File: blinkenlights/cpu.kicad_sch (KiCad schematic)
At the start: 13 parts, among them J501 Conn_ARM_SWD, J502 USB4085-GF-A_REVA4, U501 ATSAM4S8CB-AN, U502 PCA9306DP

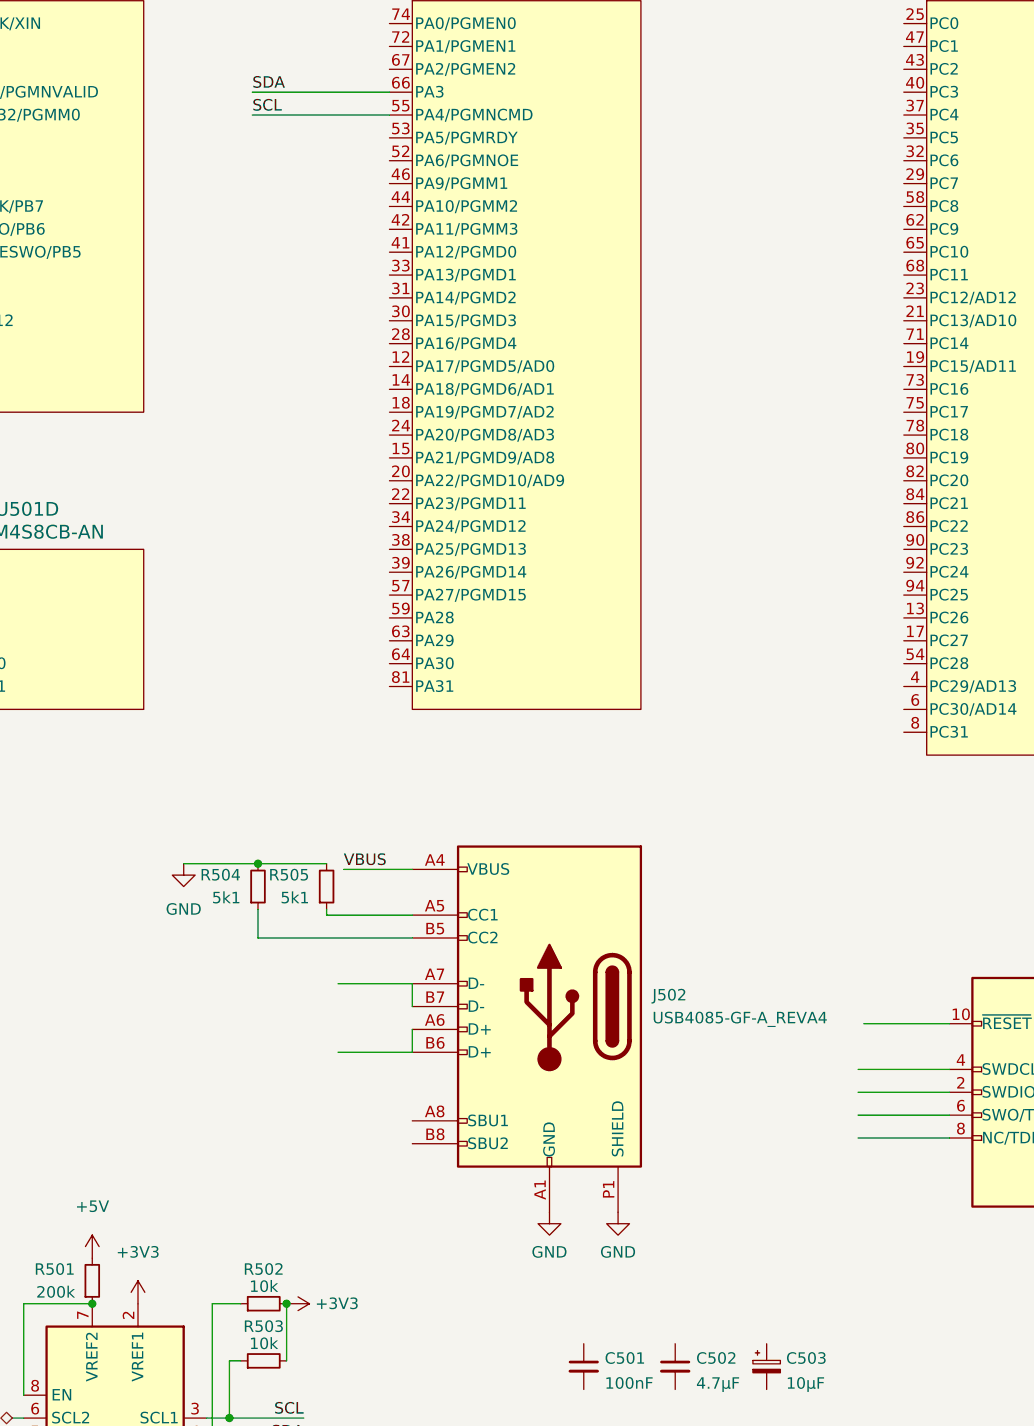
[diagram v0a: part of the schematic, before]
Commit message: removed usb that shit's whack yo
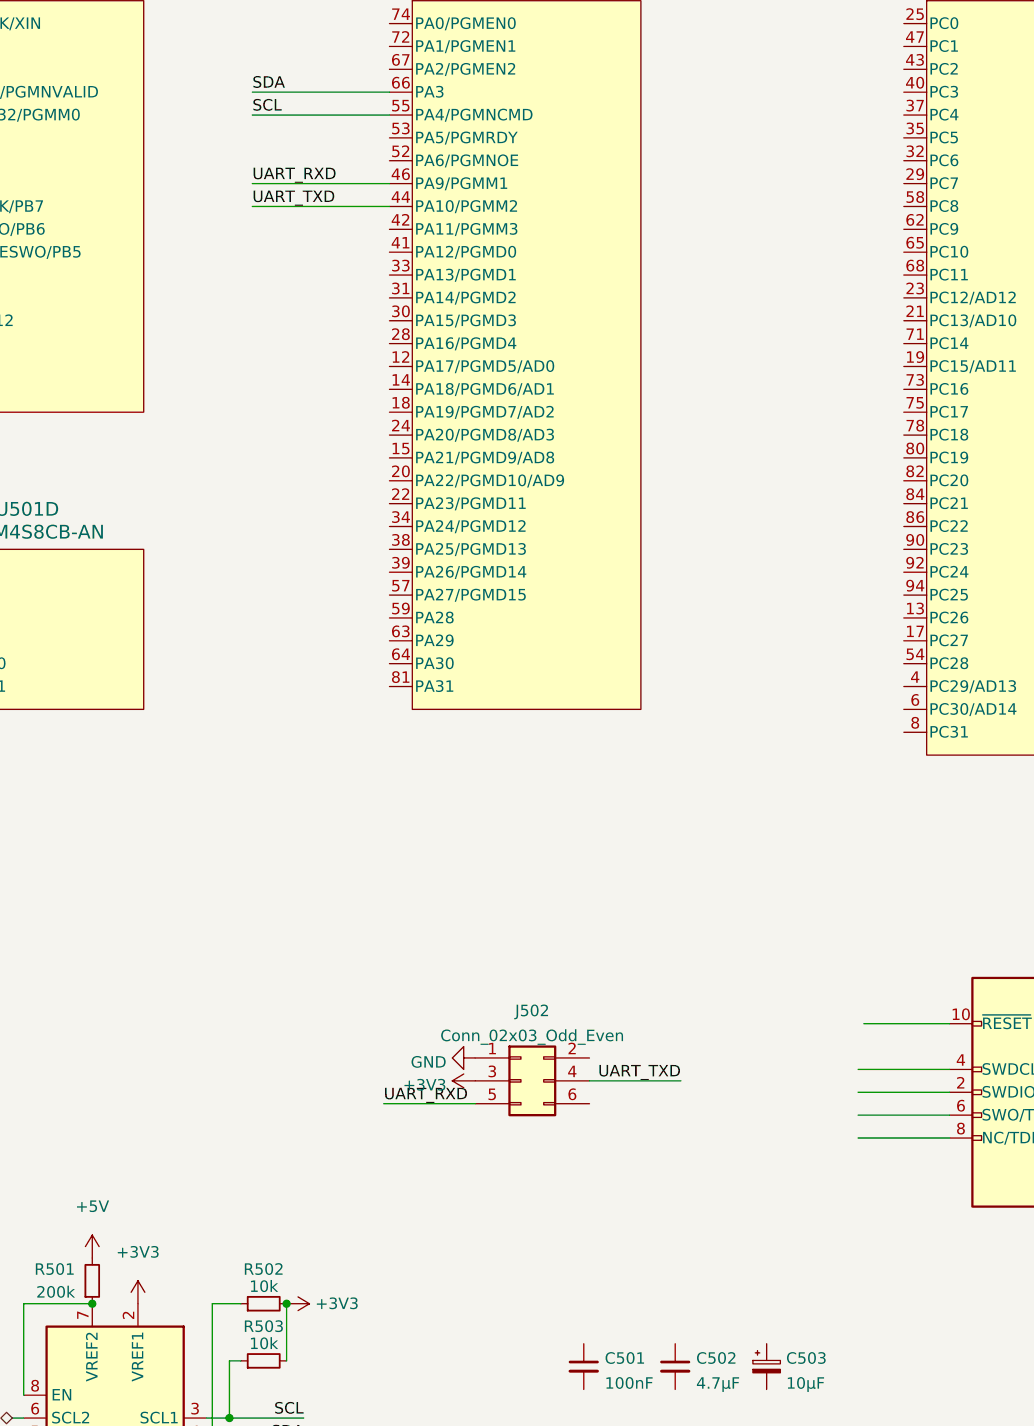
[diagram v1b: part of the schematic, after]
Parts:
- removed J502: USB4085-GF-A_REVA4, 68komputer-common:GCT_USB4085-GF-A_REVA4, symbol 68komputer-common:USB4085-GF-A_REVA4
- removed R504, R505: 5k1, symbol Device:R_Small
- added J502: Conn_02x03_Odd_Even, Connector_PinHeader_2.54mm:PinHeader_2x03_P2.54mm_Vertical, symbol Connector_Generic:Conn_02x03_Odd_Even
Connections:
- net +3V3: now also J502.3 (Pin_3)
- net GND: now also J502.1 (Pin_1)
- net UART_TXD: now reaches U501.44 (PA10/PGMM2)
- net UART_TXD: now also J502.4 (Pin_4)
- net UART_RXD: now reaches U501.46 (PA9/PGMM1)
- net UART_RXD: now also J502.5 (Pin_5)

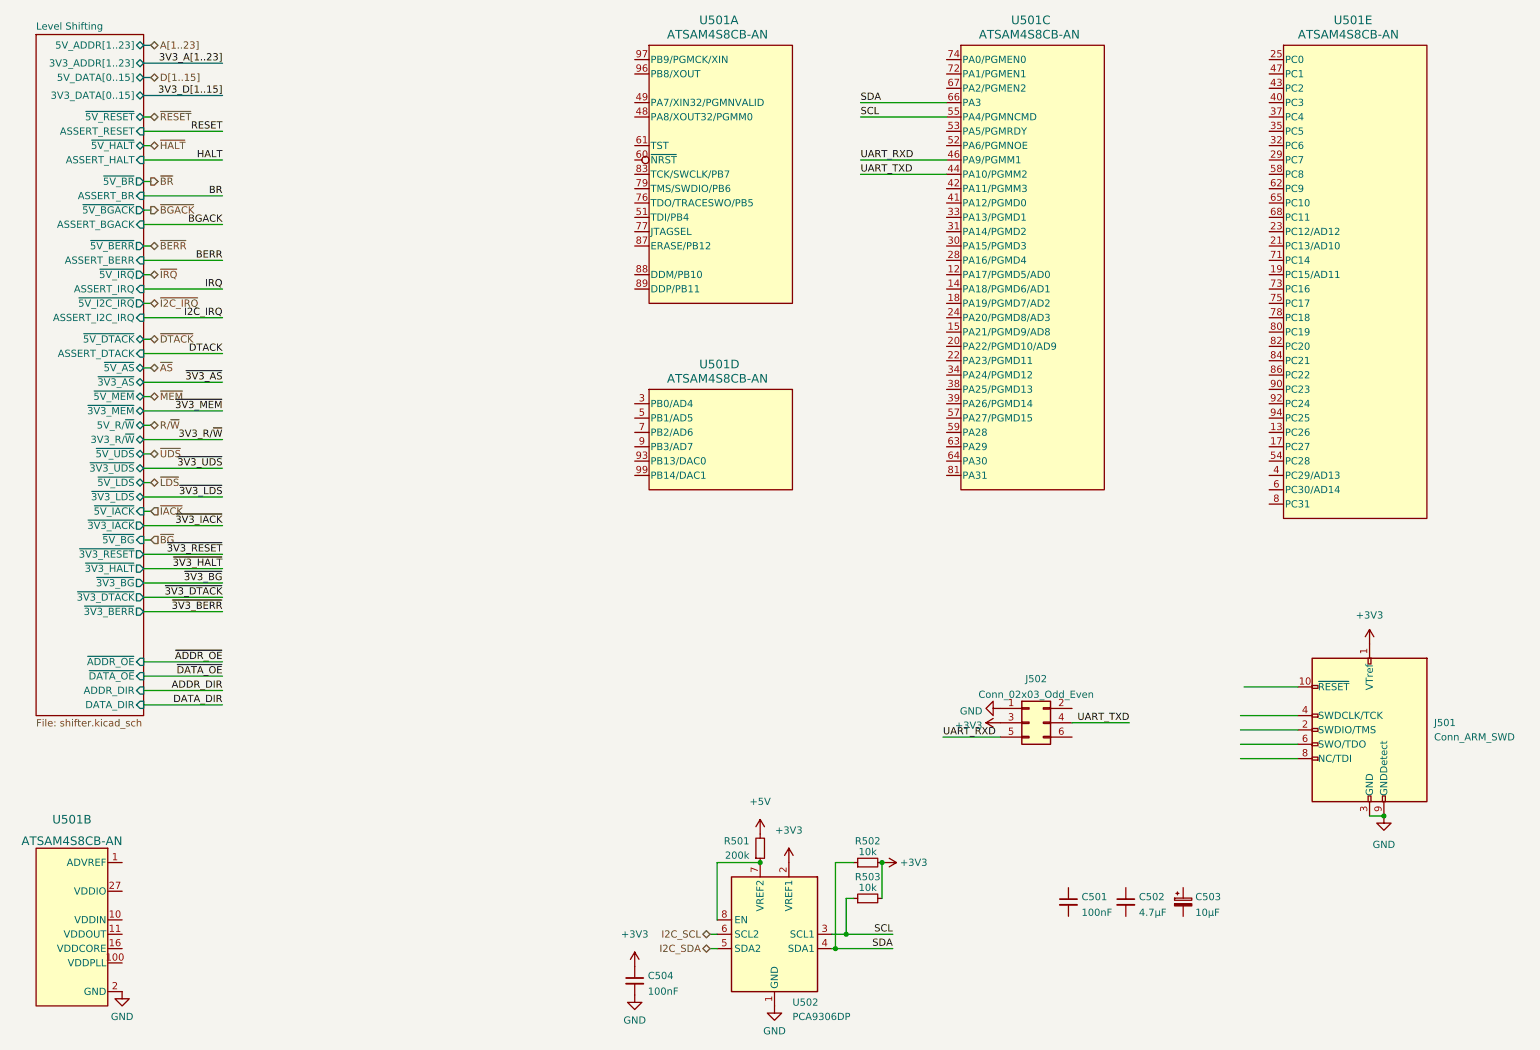
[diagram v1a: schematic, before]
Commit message: Routed address/data bus on blinkenlights
- It goes to the funky hex display bois now and is routed so that it
  should be pretty ez to yeet on down into level shifters for the big
  ARM chip that runs the show
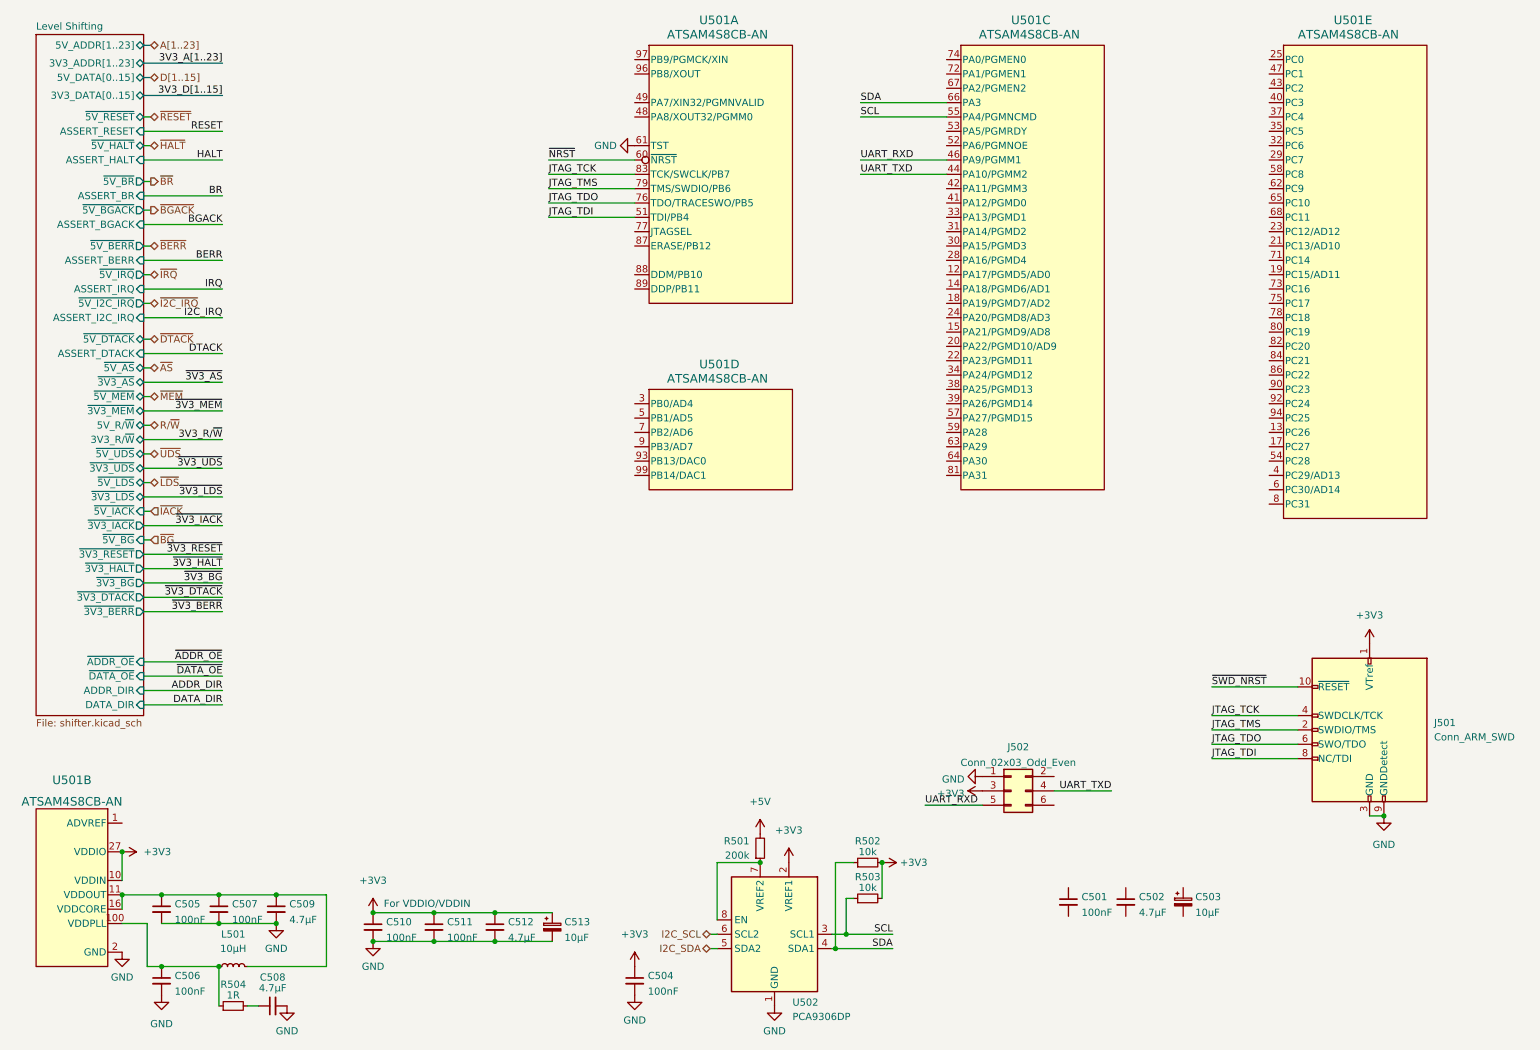
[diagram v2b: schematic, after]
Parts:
- added C505, C506, C507, C510, C511: 100nF, Capacitor_SMD:C_0805_2012Metric, symbol Device:C_Small
- added C508, C509, C512: 4.7µF, Capacitor_SMD:C_0805_2012Metric, symbol Device:C_Small
- added C513: 10µF, Capacitor_Tantalum_SMD:CP_EIA-3528-21_Kemet-B, symbol Device:C_Polarized_Small
- added L501: 10µH, Inductor_SMD:L_0805_2012Metric, symbol Device:L_Small
- added R504: 1R, Resistor_SMD:R_0805_2012Metric, symbol Device:R_Small
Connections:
- net VDDIO is gone; now on net +3V3: U501.27 (VDDIO), U501.50 (VDDIO), U501.69 (VDDIO), U501.91 (VDDIO), U501.98 (VDDIO)
- net +3V3: now also U501.10 (VDDIN), C510.1, C511.1, C512.1, C513.1
- net GND: now also U501.61 (TST), C505.2, C506.2, C507.2, C508.2, C509.2, C510.2, C511.2, C512.2, C513.2
- net VDDCORE: now also U501.11 (VDDOUT), C505.1, C507.1, C509.1, L501.2
- net at U501.100 (VDDPLL): now also C506.1, L501.1, R504.1
- net JTAG_TDI: now reaches U501.51 (TDI/PB4)
- net JTAG_TDI: now also J501.8 (NC/TDI)
- net ~{NRST}: now reaches U501.60 (~{NRST})
- net JTAG_TDO: now reaches U501.76 (TDO/TRACESWO/PB5)
- net JTAG_TDO: now also J501.6 (SWO/TDO)
- net JTAG_TMS: now reaches U501.79 (TMS/SWDIO/PB6)
- net JTAG_TMS: now also J501.2 (SWDIO/TMS)
- net JTAG_TCK: now reaches U501.83 (TCK/SWCLK/PB7)
- net JTAG_TCK: now also J501.4 (SWDCLK/TCK)
- net ~{SWD_NRST}: now reaches J501.10 (~{RESET})
- new net: C508.1, R504.2
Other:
- note added: "For VDDIO/VDDIN"
- moved on the sheet: J502, U501B
